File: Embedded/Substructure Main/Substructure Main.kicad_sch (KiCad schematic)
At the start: 0 parts

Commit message: Added PCB Ideation
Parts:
- added BootSW1: SW_Push, Button-R-667843:Button-R-667843, symbol Switch:SW_Push
- added C1: 1uF, Capacitor_SMD:C_0603_1608Metric, symbol Device:C
- added C2: 22uF, Capacitor_SMD:C_0603_1608Metric_Pad1.08x0.95mm_HandSolder, symbol Device:C
- added C3: 0.1uF, Capacitor_SMD:C_0603_1608Metric_Pad1.08x0.95mm_HandSolder, symbol Device:C
- added ESP1: ESP32-S3-WROOM-1, PCM_Espressif:ESP32-S3-WROOM-1, symbol PCM_Espressif:ESP32-S3-WROOM-1
- added R1, R2: 10K, Resistor_SMD:R_0603_1608Metric, symbol Device:R
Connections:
- new net: BootSW1.1, ESP1.27 (GPIO0/BOOT), R2.2
- new net: C1.2, ESP1.3 (EN), R1.2
- new net +3V3: C2.1, C3.1, ESP1.2 (3V3), R1.1, R2.1
- new net GND: BootSW1.2, C1.1, C2.2, C3.2, ESP1.1 (GND), ESP1.40 (GND), ESP1.41 (GND)
- new net USB +: ESP1.14 (GPIO20/U1CTS/ADC2_CH9/CLK_OUT1/USB_D+)
- new net USB -: ESP1.13 (GPIO19/U1RTS/ADC2_CH8/CLK_OUT2/USB_D-)
- no-connect marks 0 -> 3

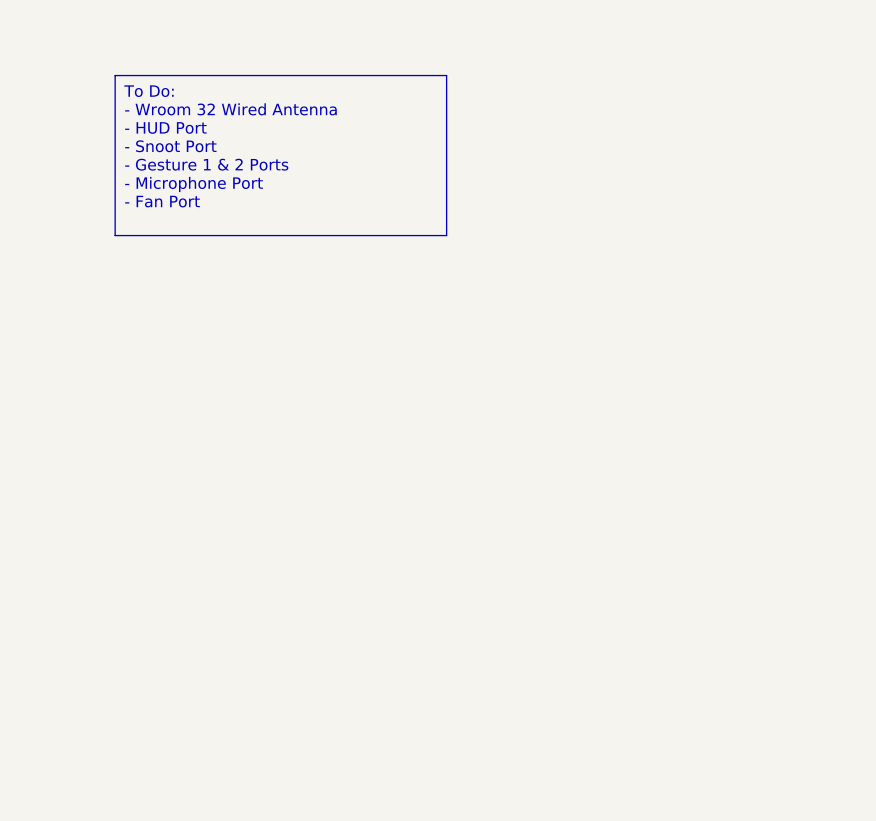
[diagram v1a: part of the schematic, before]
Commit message: Modified Schematic to use correct library
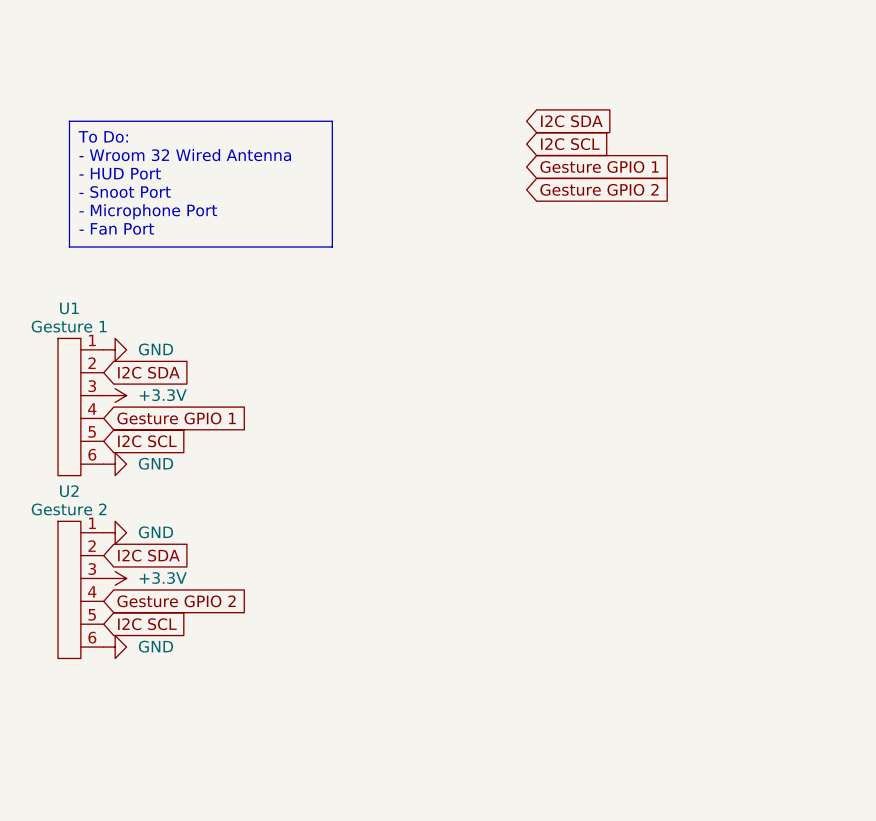
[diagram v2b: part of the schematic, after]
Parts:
- added U1: Gesture 1, FFC:FFC-6-0.5, symbol FFC:FFC-6
- added U2: Gesture 2, FFC:FFC-6-0.5, symbol FFC:FFC-6
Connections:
- net GND: now also U1.1, U1.6, U2.1, U2.6
- new net +3.3V: U1.3, U2.3
- new net Gesture GPIO 1: U1.4
- new net Gesture GPIO 2: U2.4
- new net I2C SCL: U1.5, U2.5
- new net I2C SDA: U1.2, U2.2

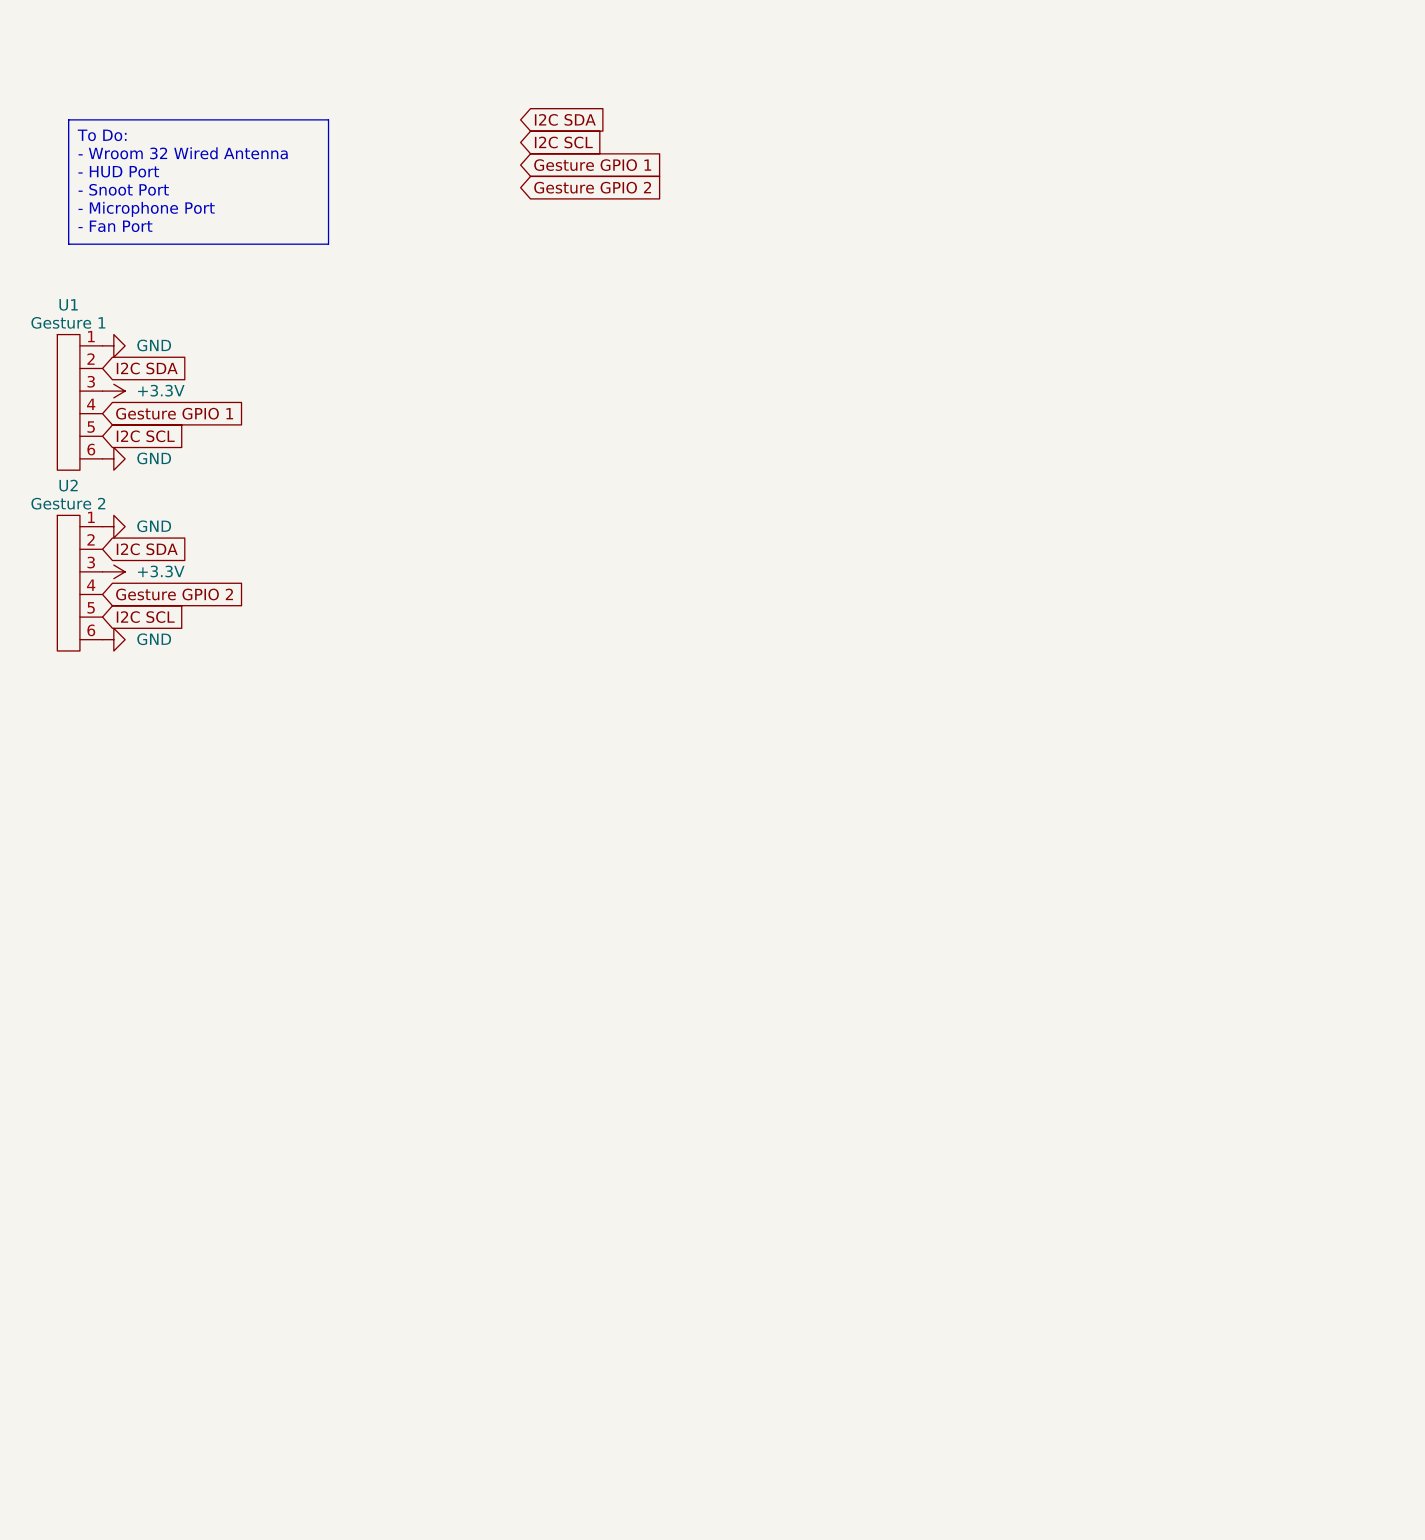
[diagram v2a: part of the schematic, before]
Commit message: Added Ports
Main to Snoot
Power to Main
Main to HUD
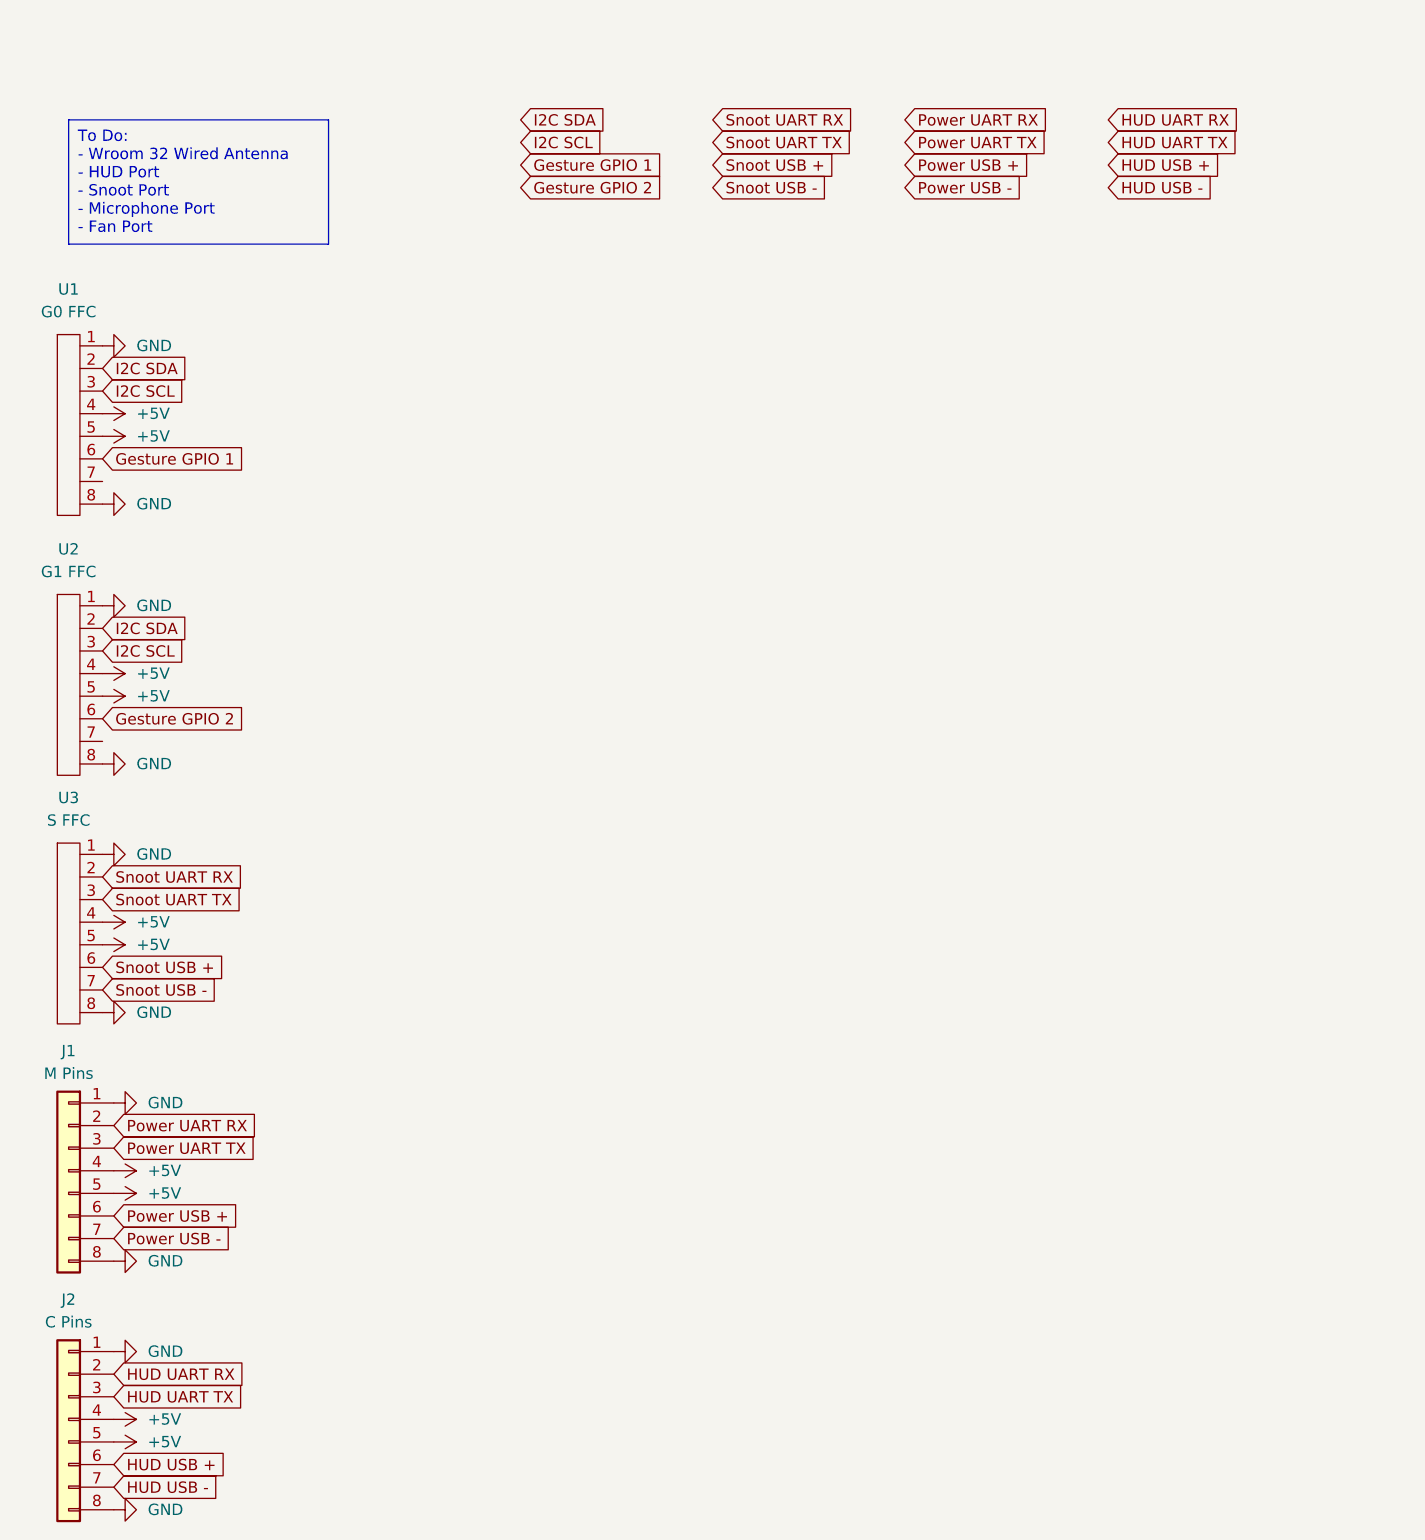
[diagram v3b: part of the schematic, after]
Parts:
- removed U1: Gesture 1, FFC:FFC-6-0.5, symbol FFC:FFC-6
- removed U2: Gesture 2, FFC:FFC-6-0.5, symbol FFC:FFC-6
- added J1: M Pins, symbol Connector_Generic:Conn_01x08
- added J2: C Pins, symbol Connector_Generic:Conn_01x08
- added U1: G0 FFC, FFC:FFC-8-0.5, symbol FFC:FFC-8
- added U2: G1 FFC, FFC:FFC-8-0.5, symbol FFC:FFC-8
- added U3: S FFC, FFC:FFC-8-0.5, symbol FFC:FFC-8
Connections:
- net GND: now also J1.1 (Pin_1), J1.8 (Pin_8), J2.1 (Pin_1), J2.8 (Pin_8), U1.1, U1.8, U2.1, U2.8, U3.1, U3.8
- net Gesture GPIO 1: now also U1.6
- net Gesture GPIO 2: now also U2.6
- net I2C SCL: now also U1.3, U2.3
- net I2C SDA: now also U1.2, U2.2
- new net +5V: J1.4 (Pin_4), J1.5 (Pin_5), J2.4 (Pin_4), J2.5 (Pin_5), U1.4, U1.5, U2.4, U2.5, U3.4, U3.5
- new net HUD UART RX: J2.2 (Pin_2)
- new net HUD UART TX: J2.3 (Pin_3)
- new net HUD USB +: J2.6 (Pin_6)
- new net HUD USB -: J2.7 (Pin_7)
- new net Power UART RX: J1.2 (Pin_2)
- new net Power UART TX: J1.3 (Pin_3)
- new net Power USB +: J1.6 (Pin_6)
- new net Power USB -: J1.7 (Pin_7)
- new net Snoot UART RX: U3.2
- new net Snoot UART TX: U3.3
- new net Snoot USB +: U3.6
- new net Snoot USB -: U3.7
